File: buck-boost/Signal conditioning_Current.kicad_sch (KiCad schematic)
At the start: 13 parts, among them U15 Opamp_Dual

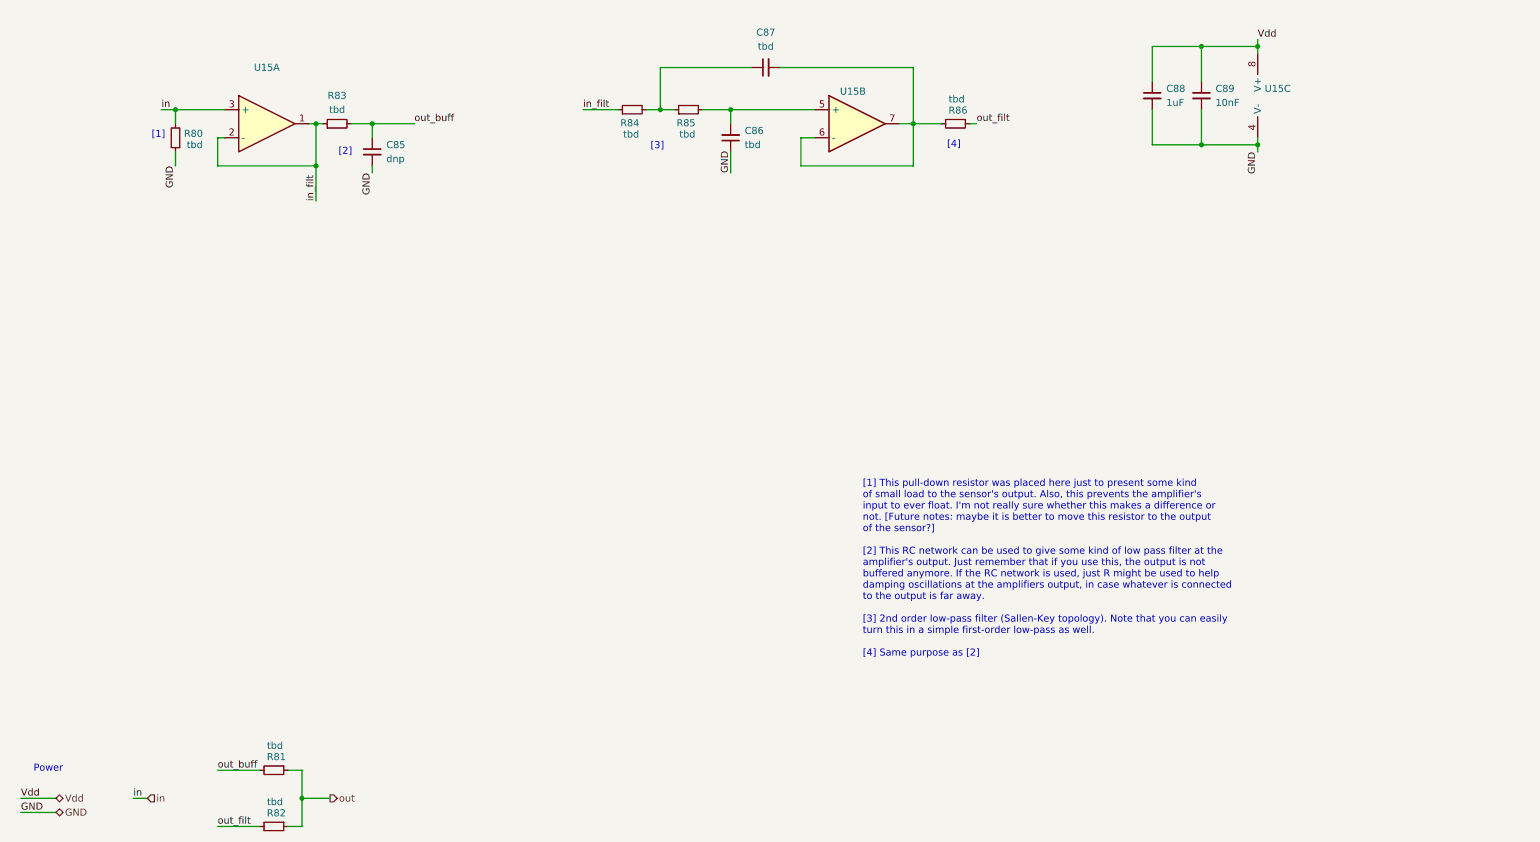
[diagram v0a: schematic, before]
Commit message: The changes indicated in the text document Review. 05.11.2024 were implemented. Missing footprints were added
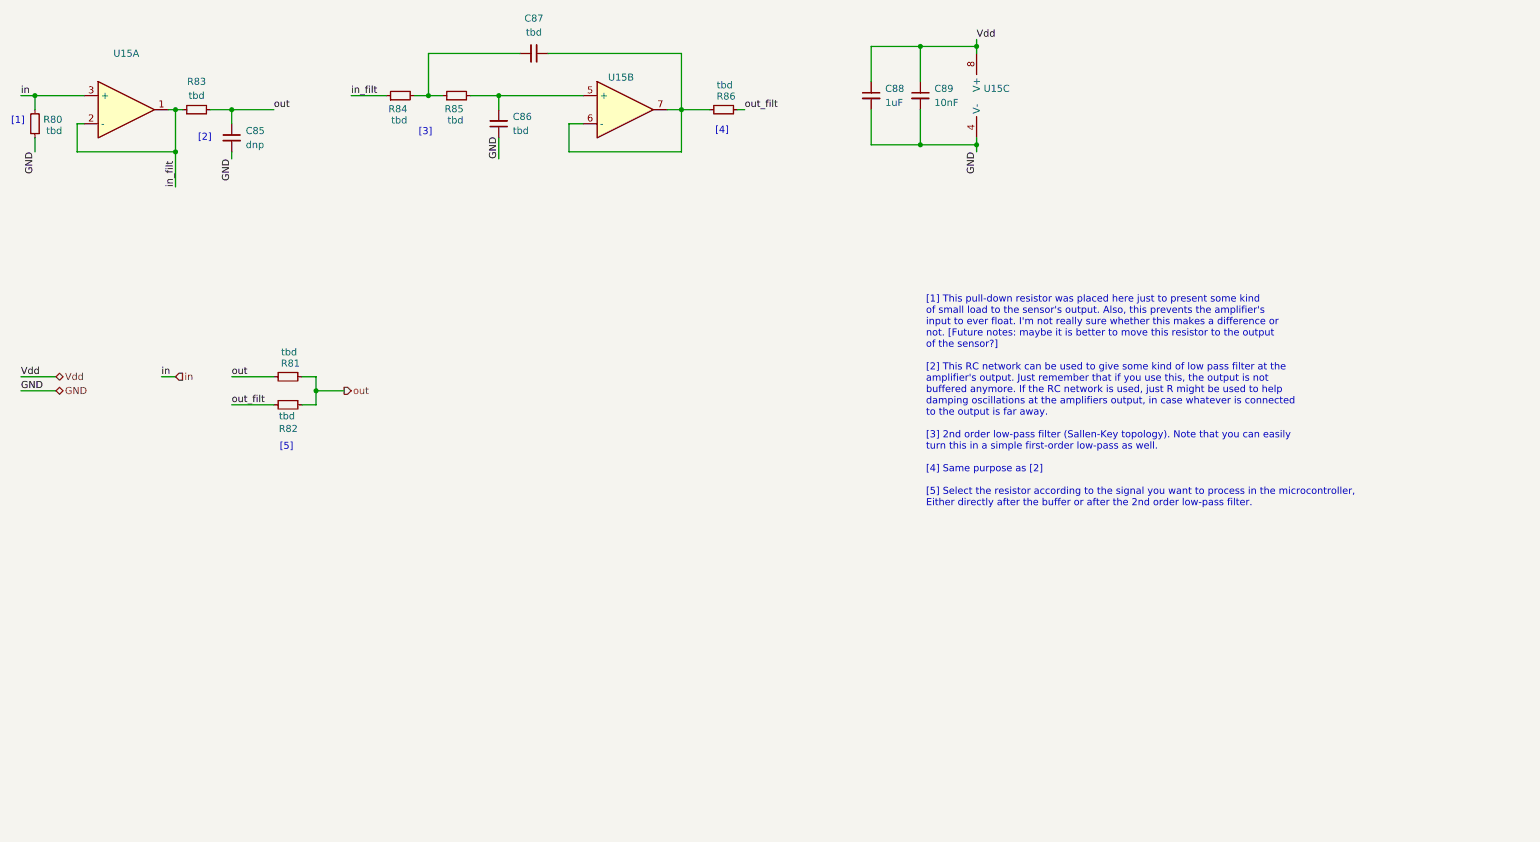
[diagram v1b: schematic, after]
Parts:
- U15: footprint (none) -> Package_SO:SOIC-8_3.9x4.9mm_P1.27mm
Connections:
- net out_buff is gone; now on net out: C85.1, R81.2, R83.2
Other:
- note added: "[5]"
- note removed: "Power"
- moved on the sheet: U15A, U15B, U15C

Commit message: Some errors in the schematics were corrected. PCB file V1.0
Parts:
- removed C88: 1uF, Capacitor_SMD:C_0805_2012Metric_Pad1.18x1.45mm_HandSolder, symbol Device:C_Small
- removed C89: 10nF, Capacitor_SMD:C_0805_2012Metric_Pad1.18x1.45mm_HandSolder, symbol Device:C_Small
- added C105: 1uF, Capacitor_SMD:C_0805_2012Metric_Pad1.18x1.45mm_HandSolder, symbol Device:C_Small
- added C106: 10nF, Capacitor_SMD:C_0805_2012Metric_Pad1.18x1.45mm_HandSolder, symbol Device:C_Small
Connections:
- net GND: now also C105.2, C106.2
- net Vdd: now also C105.1, C106.1
- net out: no longer C85.1, R81.2, R83.2
- new net out_: C85.1, R81.2, R83.2
